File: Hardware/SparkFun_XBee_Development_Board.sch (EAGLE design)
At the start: 80 parts, among them J4 QWIIC_RIGHT_ANGLE, Q2 3.1A/30V/105mΩ, U1 FSUSB30MUX_MSOP10, U2 AP63203, U3 ESD Diode, U4 MCP73831, U5 ESD Diode, U7 FT231XS

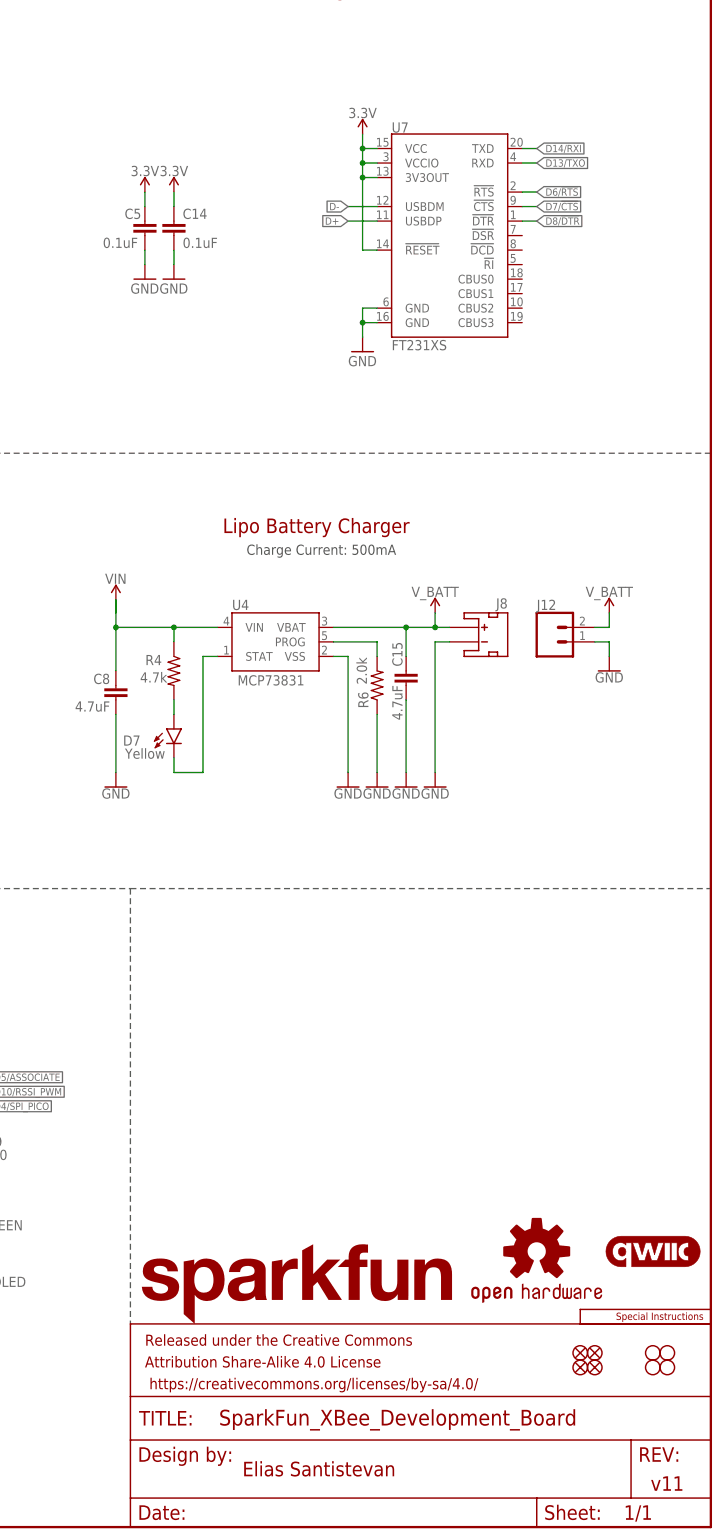
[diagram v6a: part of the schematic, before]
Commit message: Powers FTDI with VUSB
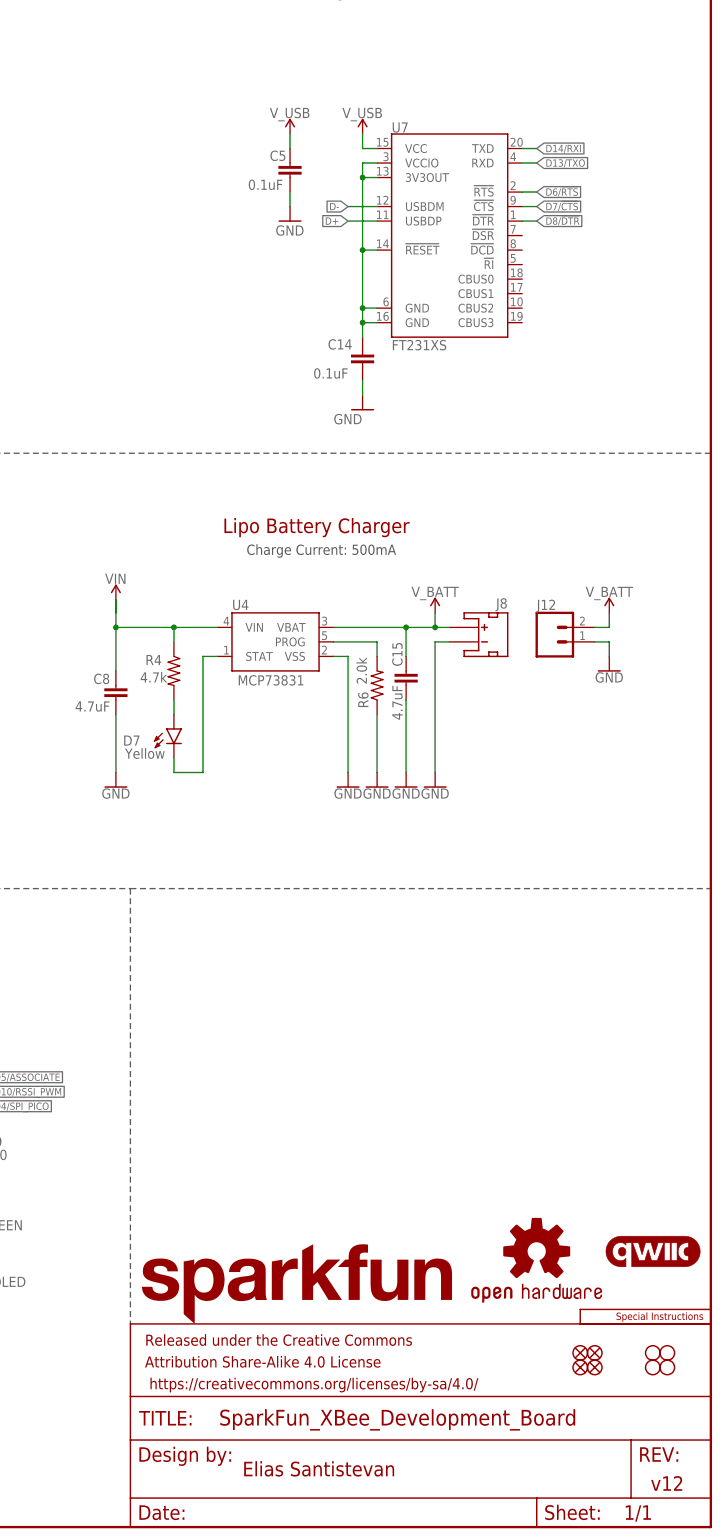
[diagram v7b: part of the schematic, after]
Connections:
- new net N$18: C14.1, U7.!RESET, U7.3V3OUT, U7.GND@16, U7.GND@6, U7.VCCIO
- net 3.3V: no longer C14.1, C5.1, U7.!RESET, U7.3V3OUT, U7.VCC, U7.VCCIO
- net GND: no longer U7.GND@16, U7.GND@6
- net V_USB: now also C5.1, U7.VCC
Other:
- note added: "v12"
- note removed: "v11"
- moved on the sheet: C14, C5
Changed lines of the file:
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@@
 <part name="GND37" library="SparkFun-PowerSymbols" deviceset="GND" device=""/>
 <part name="U7" library="SparkFun-IC-Comms" deviceset="FT231X" device="S" value="FT231XS"/>
-<part name="GND39" library="SparkFun-PowerSymbols" deviceset="GND" device=""/>
 <part name="C14" library="SparkFun-Capacitors" deviceset="0.1UF" device="-0603-25V-(+80/-20%)" value="0.1uF"/>
 <part name="C5" library="SparkFun-Capacitors" deviceset="0.1UF" device="-0603-25V-(+80/-20%)" value="0.1uF"/>
 <part name="GND30" library="SparkFun-PowerSymbols" deviceset="GND" device=""/>
-<part name="SUPPLY6" library="SparkFun-PowerSymbols" deviceset="3.3V" device=""/>
-<part name="SUPPLY21" library="SparkFun-PowerSymbols" deviceset="3.3V" device=""/>
 <part name="GND32" library="SparkFun-PowerSymbols" deviceset="GND" device=""/>
-<part name="SUPPLY22" library="SparkFun-PowerSymbols" deviceset="3.3V" device=""/>
 <part name="L1" library="SparkFun-Coils" deviceset="3.9UH" device="" value="3.9UH"/>
 <part name="U4" library="SparkFun-IC-Power" deviceset="MCP73831" device=""/>
@@
 <part name="GND42" library="SparkFun-PowerSymbols" deviceset="GND" device=""/>
 <part name="IOLED" library="SparkFun-Jumpers" deviceset="JUMPER-SMT_2_NC_TRACE" device="_SILK" package3d_urn="urn:adsk.eagle:package:39281/1"/>
+<part name="SUPPLY22" library="SparkFun-PowerSymbols" deviceset="V_USB" device=""/>
+<part name="SUPPLY6" library="SparkFun-PowerSymbols" deviceset="V_USB" device=""/>
 </parts>
 <sheets>
@@
 <wire x1="294.64" y1="187.96" x2="431.8" y2="187.96" width="0.2032" layer="97" style="longdash"/>
 <wire x1="121.92" y1="111.76" x2="121.92" y2="0" width="0.2032" layer="97" style="longdash"/>
-<text x="424.18" y="7.62" size="2.54" layer="94" font="vector" align="center">v11</text>
+<text x="424.18" y="7.62" size="2.54" layer="94" font="vector" align="center">v12</text>
 <text x="363.22" y="10.16" size="2.54" layer="94" font="vector" align="center">Elias Santistevan</text>
 <wire x1="223.52" y1="111.76" x2="223.52" y2="0" width="0.2032" layer="97" style="longdash"/>
@@
 <attribute name="VALUE" x="375.92" y="207.772" size="1.778" layer="96" align="top-left"/>
 </instance>
-<instance part="GND39" gate="1" x="370.84" y="205.74" smashed="yes">
-<attribute name="VALUE" x="368.3" y="203.2" size="1.778" layer="96" font="vector"/>
-</instance>
-<instance part="C14" gate="G$1" x="337.82" y="226.06" smashed="yes">
-<attribute name="NAME" x="339.344" y="228.981" size="1.778" layer="95" font="vector"/>
-<attribute name="VALUE" x="339.344" y="223.901" size="1.778" layer="96" font="vector"/>
-</instance>
-<instance part="C5" gate="G$1" x="332.74" y="226.06" smashed="yes">
-<attribute name="NAME" x="329.184" y="228.981" size="1.778" layer="95" font="vector"/>
-<attribute name="VALUE" x="325.374" y="223.901" size="1.778" layer="96" font="vector"/>
-</instance>
-<instance part="GND30" gate="1" x="332.74" y="218.44" smashed="yes">
-<attribute name="VALUE" x="330.2" y="215.9" size="1.778" layer="96" font="vector"/>
-</instance>
-<instance part="SUPPLY6" gate="G$1" x="332.74" y="233.68" smashed="yes">
-<attribute name="VALUE" x="332.74" y="236.474" size="1.778" layer="96" font="vector" align="bottom-center"/>
-</instance>
-<instance part="SUPPLY21" gate="G$1" x="337.82" y="233.68" smashed="yes">
-<attribute name="VALUE" x="337.82" y="236.474" size="1.778" layer="96" font="vector" align="bottom-center"/>
-</instance>
-<instance part="GND32" gate="1" x="337.82" y="218.44" smashed="yes">
-<attribute name="VALUE" x="335.28" y="215.9" size="1.778" layer="96" font="vector"/>
-</instance>
-<instance part="SUPPLY22" gate="G$1" x="370.84" y="243.84" smashed="yes">
-<attribute name="VALUE" x="370.84" y="246.634" size="1.778" layer="96" font="vector" align="bottom-center"/>
+<instance part="C14" gate="G$1" x="370.84" y="203.2" smashed="yes">
+<attribute name="NAME" x="364.744" y="206.121" size="1.778" layer="95" font="vector"/>
+<attribute name="VALUE" x="362.204" y="201.041" size="1.778" layer="96" font="vector"/>
+</instance>
+<instance part="C5" gate="G$1" x="358.14" y="236.22" smashed="yes">
+<attribute name="NAME" x="354.584" y="239.141" size="1.778" layer="95" font="vector"/>
+<attribute name="VALUE" x="350.774" y="234.061" size="1.778" layer="96" font="vector"/>
+</instance>
+<instance part="GND30" gate="1" x="358.14" y="228.6" smashed="yes">
+<attribute name="VALUE" x="355.6" y="226.06" size="1.778" layer="96" font="vector"/>
+</instance>
+<instance part="GND32" gate="1" x="370.84" y="195.58" smashed="yes">
+<attribute name="VALUE" x="365.76" y="193.04" size="1.778" layer="96" font="vector"/>
 </instance>
 <instance part="L1" gate="G$1" x="261.62" y="142.24" smashed="yes" rot="R90">
@@
 <instance part="IOLED" gate="G$1" x="302.26" y="43.18" smashed="yes" rot="R90">
 <attribute name="NAME" x="308.61" y="42.926" size="1.778" layer="95" font="vector" rot="R180" align="center"/>
+</instance>
+<instance part="SUPPLY22" gate="G$1" x="370.84" y="243.84" smashed="yes">
+<attribute name="VALUE" x="370.84" y="246.634" size="1.778" layer="96" font="vector" align="bottom-center"/>
+</instance>
+<instance part="SUPPLY6" gate="G$1" x="358.14" y="243.84" smashed="yes">
+<attribute name="VALUE" x="358.14" y="246.634" size="1.778" layer="96" font="vector" align="bottom-center"/>
 </instance>
 </instances>
@@
 <segment>
 <pinref part="C5" gate="G$1" pin="2"/>
-<wire x1="332.74" y1="220.98" x2="332.74" y2="223.52" width="0.1524" layer="91"/>
+<wire x1="358.14" y1="231.14" x2="358.14" y2="233.68" width="0.1524" layer="91"/>
 <pinref part="GND30" gate="1" pin="GND"/>
 </segment>
 <segment>
 <pinref part="C14" gate="G$1" pin="2"/>
-<wire x1="337.82" y1="223.52" x2="337.82" y2="220.98" width="0.1524" layer="91"/>
+<wire x1="370.84" y1="200.66" x2="370.84" y2="198.12" width="0.1524" layer="91"/>
 <pinref part="GND32" gate="1" pin="GND"/>
-</segment>
-<segment>
-<pinref part="U7" gate="U$1" pin="GND@6"/>
-<wire x1="373.38" y1="213.36" x2="370.84" y2="213.36" width="0.1524" layer="91"/>
-<wire x1="370.84" y1="213.36" x2="370.84" y2="210.82" width="0.1524" layer="91"/>
-<pinref part="U7" gate="U$1" pin="GND@16"/>
-<wire x1="373.38" y1="210.82" x2="370.84" y2="210.82" width="0.1524" layer="91"/>
-<junction x="370.84" y="210.82"/>
-<wire x1="370.84" y1="210.82" x2="370.84" y2="208.28" width="0.1524" layer="91"/>
-<pinref part="GND39" gate="1" pin="GND"/>
 </segment>
 <segment>
@@
 <wire x1="68.58" y1="81.28" x2="68.58" y2="78.74" width="0.1524" layer="91"/>
 </segment>
-<segment>
-<pinref part="SUPPLY21" gate="G$1" pin="3.3V"/>
-<pinref part="C14" gate="G$1" pin="1"/>
-<wire x1="337.82" y1="231.14" x2="337.82" y2="233.68" width="0.1524" layer="91"/>
-</segment>
-<segment>
-<pinref part="SUPPLY6" gate="G$1" pin="3.3V"/>
-<pinref part="C5" gate="G$1" pin="1"/>
-<wire x1="332.74" y1="231.14" x2="332.74" y2="233.68" width="0.1524" layer="91"/>
-</segment>
-<segment>
-<pinref part="U7" gate="U$1" pin="VCCIO"/>
-<wire x1="373.38" y1="238.76" x2="370.84" y2="238.76" width="0.1524" layer="91"/>
-<wire x1="370.84" y1="238.76" x2="370.84" y2="241.3" width="0.1524" layer="91"/>
-<pinref part="U7" gate="U$1" pin="VCC"/>
-<wire x1="370.84" y1="241.3" x2="370.84" y2="243.84" width="0.1524" layer="91"/>
-<wire x1="373.38" y1="241.3" x2="370.84" y2="241.3" width="0.1524" layer="91"/>
-<junction x="370.84" y="241.3"/>
-<junction x="370.84" y="238.76"/>
-<pinref part="U7" gate="U$1" pin="!RESET"/>
-<wire x1="370.84" y1="223.52" x2="370.84" y2="236.22" width="0.1524" layer="91"/>
-<wire x1="370.84" y1="236.22" x2="370.84" y2="238.76" width="0.1524" layer="91"/>
-<wire x1="373.38" y1="223.52" x2="370.84" y2="223.52" width="0.1524" layer="91"/>
-<pinref part="U7" gate="U$1" pin="3V3OUT"/>
-<wire x1="373.38" y1="236.22" x2="370.84" y2="236.22" width="0.1524" layer="91"/>
-<junction x="370.84" y="236.22"/>
-<pinref part="SUPPLY22" gate="G$1" pin="3.3V"/>
-</segment>
 </net>
 <net name="V_USB" class="0">
@@
 <pinref part="SUPPLY16" gate="G$1" pin="V_USB"/>
 <wire x1="182.88" y1="251.46" x2="182.88" y2="254" width="0.1524" layer="91"/>
+</segment>
+<segment>
+<pinref part="U7" gate="U$1" pin="VCC"/>
+<pinref part="SUPPLY22" gate="G$1" pin="V_USB"/>
+<wire x1="373.38" y1="241.3" x2="370.84" y2="241.3" width="0.1524" layer="91"/>
+<wire x1="370.84" y1="241.3" x2="370.84" y2="243.84" width="0.1524" layer="91"/>
+</segment>
+<segment>
+<pinref part="C5" gate="G$1" pin="1"/>
+<pinref part="SUPPLY6" gate="G$1" pin="V_USB"/>
+<wire x1="358.14" y1="241.3" x2="358.14" y2="243.84" width="0.1524" layer="91"/>
 </segment>
 </net>
@@
 </segment>
 </net>
+<net name="N$18" class="0">
+<segment>
+<pinref part="U7" gate="U$1" pin="GND@16"/>
+<pinref part="C14" gate="G$1" pin="1"/>
+<wire x1="373.38" y1="210.82" x2="370.84" y2="210.82" width="0.1524" layer="91"/>
+<wire x1="370.84" y1="210.82" x2="370.84" y2="208.28" width="0.1524" layer="91"/>
+<pinref part="U7" gate="U$1" pin="GND@6"/>
+<wire x1="373.38" y1="213.36" x2="370.84" y2="213.36" width="0.1524" layer="91"/>
+<wire x1="370.84" y1="213.36" x2="370.84" y2="210.82" width="0.1524" layer="91"/>
+<junction x="370.84" y="210.82"/>
+<wire x1="370.84" y1="213.36" x2="370.84" y2="223.52" width="0.1524" layer="91"/>
+<junction x="370.84" y="213.36"/>
+<pinref part="U7" gate="U$1" pin="!RESET"/>
+<wire x1="370.84" y1="223.52" x2="373.38" y2="223.52" width="0.1524" layer="91"/>
+<pinref part="U7" gate="U$1" pin="VCCIO"/>
+<wire x1="373.38" y1="238.76" x2="370.84" y2="238.76" width="0.1524" layer="91"/>
+<wire x1="370.84" y1="236.22" x2="370.84" y2="238.76" width="0.1524" layer="91"/>
+<pinref part="U7" gate="U$1" pin="3V3OUT"/>
+<wire x1="373.38" y1="236.22" x2="370.84" y2="236.22" width="0.1524" layer="91"/>
+<wire x1="370.84" y1="223.52" x2="370.84" y2="236.22" width="0.1524" layer="91"/>
+<junction x="370.84" y="223.52"/>
+<junction x="370.84" y="236.22"/>
+</segment>
+</net>
